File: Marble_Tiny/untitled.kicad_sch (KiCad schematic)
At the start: 71 parts, among them Q3 XTAL_25MHZ_TXC_8Y-25.000MAAJ-T, U12 LP5951MF-3.0/NOPB, U13 LM336M-2.5, U14 DAC8550IDGK, U15 DAC8550IDGK, U16 CDCM61004RHB, U3 Si5351A-B-GT, Y1 OSC_25MHZ_RAKON_IVT3205CR, Y2 VM53S3-25.000-2.5/-30+75, Y3 OSC_20MHZ_IQD_LFVCXO026156

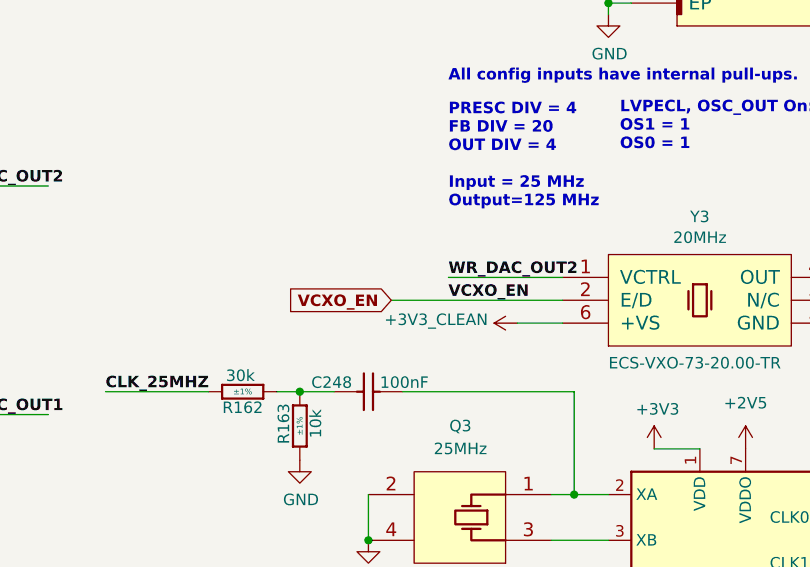
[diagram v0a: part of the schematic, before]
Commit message: fixed ERCs; added test points; added WP switch
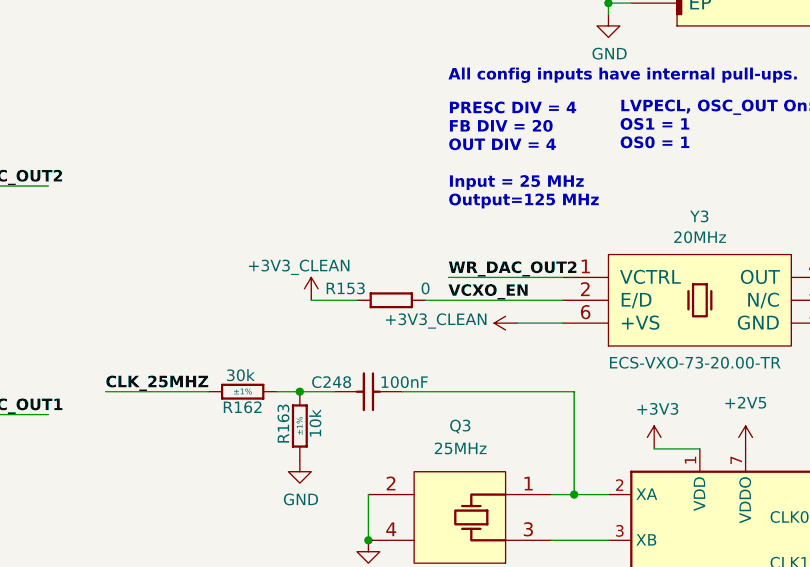
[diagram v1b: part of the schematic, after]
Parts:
- added R153: R0402_0R_JUMPER, RESC1005X40N, symbol Resistors_SMD:R0402_0R_JUMPER
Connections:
- net +3V3_CLEAN: now also R153.1
- net VCXO_EN: now also R153.2

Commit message: fixed issue with PMODs; added board name and revision; fixed polygons issue
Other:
- company: (none) -> ${name}
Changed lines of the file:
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@@
 	(generator_version "9.0")
 	(paper "A4")
+	(title_block
+		(date "2025-04-18")
+		(rev "${rev}")
+		(company "${name}")
+		(comment 1 "${author}")
+	)
 	(text "1"
 		(exclude_from_sim no)
